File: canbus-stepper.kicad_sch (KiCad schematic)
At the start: 63 parts, among them J1 TYPE-C USB SOCKET, J2 Motor Output, J3 CAN Daisy-Chain 1, J4 CAN Daisy-Chain 2, J5 Qwiic I2C, J6 AUX Port, J7 SFV30R-2STBE1HLF (30-Pin OLED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, J8 24V Power Input Terminal, J9 24V Power Output Terminal, Q1 AO4407A, SW1 SW_Push, SW2 SW_Push, SW3 SW_Push, SW4 SW_Push, U1 ESP32-S3-WROOM-1, U2 TMC2209, U3 AS5600-ASOT, U4 TCAN1051VDRBTQ1, U5 MP2315, U6 AP2112K-3.3TRG1, U7 USBLC6-2SC6

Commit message: chore: save board and schematic progress before autoplacer development
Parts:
- added SW5: Termination, CANBUS-Stepper:SW_TS31-46-35-BK-B-160-RA-SMT-TR, symbol Switch:SW_Push
- U1: value ESP32-S3-WROOM-1 -> ESP32-S3-MINI-1; symbol MCU_Module:ESP32-S3-WROOM-1 -> MCU_Module:ESP32-S3-MINI-1
- U4: symbol Interface_CAN:SN65HVD230 -> Interface_CAN:TCAN1051
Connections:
- net CAN_VREF is gone; now on net +3V3: U4.5 (VIO)
- net MS1 is gone; now on net GND: U2.9 (MS1)
- net MS2 is gone; now on net GND: U2.10 (MS2)
- net +3V3: now also U1.3 (3V3), U6.5 (VOUT); no longer U1.2 (3V3), U4.3 (VCC), U6.4 (VOUT)
- net +5V: now also U4.3 (VCC)
- net AUX1: now also U1.19 (IO14); no longer U1.22 (IO14)
- net AUX2: now also U1.18 (IO13); no longer U1.21 (IO13)
- net CANL: now also SW5.2
- net CAN_RX: now also U1.28 (IO47); no longer U1.24 (IO47)
- net CAN_STB: now also U1.37 (IO37); no longer U1.30 (IO37)
- net CAN_TERM_SW: now also SW5.1
- net CAN_TX: now also U1.31 (IO48); no longer U1.25 (IO48)
- net DIAG: now also U1.21 (IO16); no longer U1.9 (IO16)
- net DIR: now also U1.10 (IO6); no longer U1.6 (IO6)
- net DISABLE_3V3: now also U1.38 (IO38); no longer U1.31 (IO38)
- net EN: now also U1.39 (EN); no longer U1.3 (EN)
- net ENC_OUT_N: now also U3.5 (OUT_N); no longer U3.3 (OUT_N)
- net ENC_OUT_P: now also U3.3 (OUT_P); no longer U3.2 (OUT_P)
- net GND: now also U1.16 (GND), U3.2 (MODE); no longer U1.40 (GND), U1.41 (GND_PAD), U3.5 (GND)
- net INDEX: now also U1.15 (IO11); no longer U1.19 (IO11)
- net IO0: now also U1.4 (IO0); no longer U1.27 (IO0)
- net IO46: now also U1.46 (GND); no longer U1.16 (IO46)
- net LED1: now also U1.14 (IO10); no longer U1.18 (IO10)
- net LED2: now also U1.17 (IO12); no longer U1.20 (IO12)
- net NTC_SENSE: now also U1.11 (IO7); no longer U1.7 (IO7)
- net SCL: now also U1.13 (IO9), U3.7 (SCL); no longer U1.17 (IO9), U3.6 (SCL)
- net SDA: now also U3.6 (SDA); no longer U3.7 (SDA)
- net STEP: now also U1.9 (IO5); no longer U1.5 (IO5)
- net SW1: now also U1.35 (IO35); no longer U1.28 (IO35)
- net SW2: now also U1.36 (IO36); no longer U1.29 (IO36)
- net TMC_EN: now also U1.26 (NC); no longer U1.23 (IO21)
- net TMC_RX: now also U1.23 (IO18); no longer U1.11 (IO18)
- net TMC_TX: now also U1.22 (IO17); no longer U1.10 (IO17)
- net USB_D+: now also U1.25 (IO20); no longer U1.14 (IO20)
- net USB_D-: now also U1.24 (IO19); no longer U1.13 (IO19)
- net VBUS_SENSE: now also U1.8 (NC); no longer U1.4 (IO4)
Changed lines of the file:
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@@
 		)
 	)
-	(label "MS1"
+	(label "GND"
 		(at 299.72 76.2 0)
 		(effects
@@
 		)
 	)
-	(label "MS2"
+	(label "GND"
 		(at 299.72 78.74 0)
 		(effects
@@
 		)
 	)
-	(label "CAN_VREF"
+	(label "+3V3"
 		(at 326.07 199.23 0)
 		(effects
@@
 	)
 	(symbol
-		(lib_id "Interface_CAN:SN65HVD230")
+		(lib_id "Interface_CAN:TCAN1051")
 		(at 315.91 194.15 0)
 		(unit 1)
@@
 	)
 	(symbol
-		(lib_id "power:+3V3")
+		(lib_id "power:+5V")
 		(at 305.75 199.23 0)
 		(unit 1)
@@
 			)
 		)
-		(property "Value" "+3V3"
+		(property "Value" "+5V"
 			(at 305.75 196.23 0)
 			(show_name no)
@@
 	)
 	(symbol
-		(lib_id "MCU_Module:ESP32-S3-WROOM-1")
+		(lib_id "MCU_Module:ESP32-S3-MINI-1")
 		(at 152.4 85.09 0)
 		(unit 1)
@@
 			)
 		)
-		(property "Value" "ESP32-S3-WROOM-1"
+		(property "Value" "ESP32-S3-MINI-1"
 			(at 152.4 100.09 0)
 			(show_name no)
@@
 	(label "+24V_IN" (at 80.01 194.31 0) (effects (font (size 1.27 1.27))))
 	(label "USB_VBUS_RAW" (at 65.73 83.98 0) (effects (font (size 1.27 1.27))))
+	(symbol
+		(lib_id "Switch:SW_Push")
+		(at 350 197.96 0)
+		(unit 1)
+		(body_style 1)
+		(exclude_from_sim no)
+		(in_bom yes)
+		(on_board yes)
+		(in_pos_files yes)
+		(dnp no)
+		(property "Reference" "SW5"
+			(at 350 182.96 0)
+			(show_name no)
+			(do_not_autoplace no)
+			(effects
+				(font
+					(size 1.27 1.27)
+				)
+			)
+		)
+		(property "Value" "Termination"
+			(at 350 212.96 0)
+			(show_name no)
+			(do_not_autoplace no)
+			(effects
+				(font
+					(size 1.27 1.27)
+				)
+			)
+		)
+		(property "Footprint" "CANBUS-Stepper:SW_TS31-46-35-BK-B-160-RA-SMT-TR"
+			(at 350 197.96 0)
+			(hide yes)
+			(show_name no)
+			(do_not_autoplace no)
+			(effects
+				(font
+					(size 1.27 1.27)
+				)
+			)
+		)
+		(property "Datasheet" "~"
+			(at 350 197.96 0)
+			(hide yes)
+			(show_name no)
+			(do_not_autoplace no)
+			(effects
+				(font
+					(size 1.27 1.27)
+				)
+			)
+		)
+		(property "Description" "CAN Bus 120R Termination Switch"
+			(at 350 197.96 0)
+			(show_name no)
+			(do_not_autoplace no)
+			(effects
+				(font
+					(size 1.27 1.27)
+				)
+			)
+		)
+		(pin "1"
+		)
+		(pin "2"
+		)
+		(instances
+			(project "canbus-stepper"
+				(path "/708095da-6de2-439a-99a4-e77d5d456b3f"
+					(reference "SW5")
+					(unit 1)
+				)
+			)
+		)
+	)
+	(label "CAN_TERM_SW"
+		(at 344.92 197.96 0)
+		(effects
+			(font
+				(size 1.27 1.27)
+			)
+		)
+	)
+	(label "CANL"
+		(at 355.08 197.96 0)
+		(effects
+			(font
+				(size 1.27 1.27)
+			)
+		)
+	)
 )

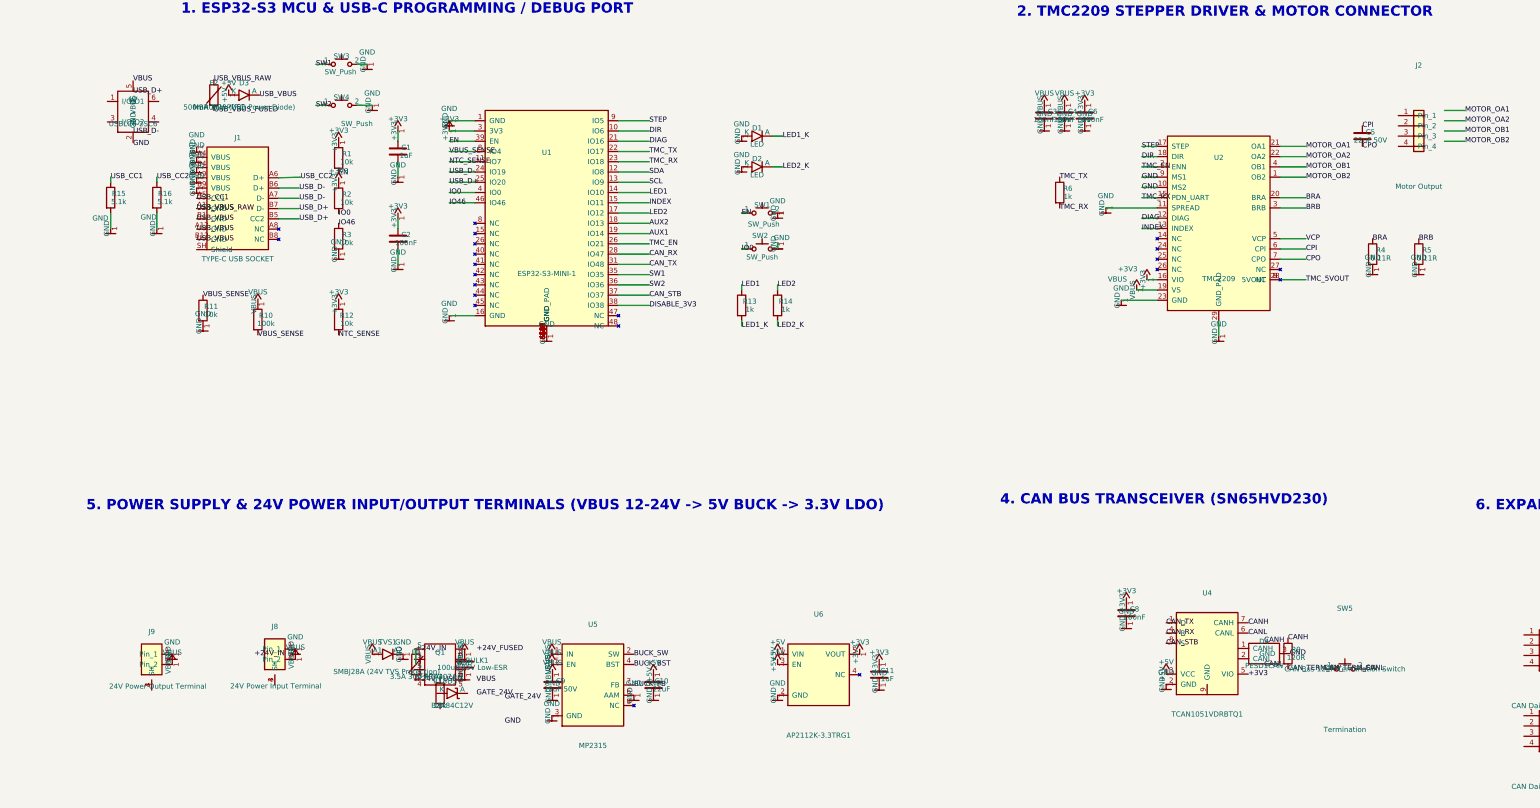
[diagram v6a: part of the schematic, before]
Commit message: update canbus ohm sw footprint
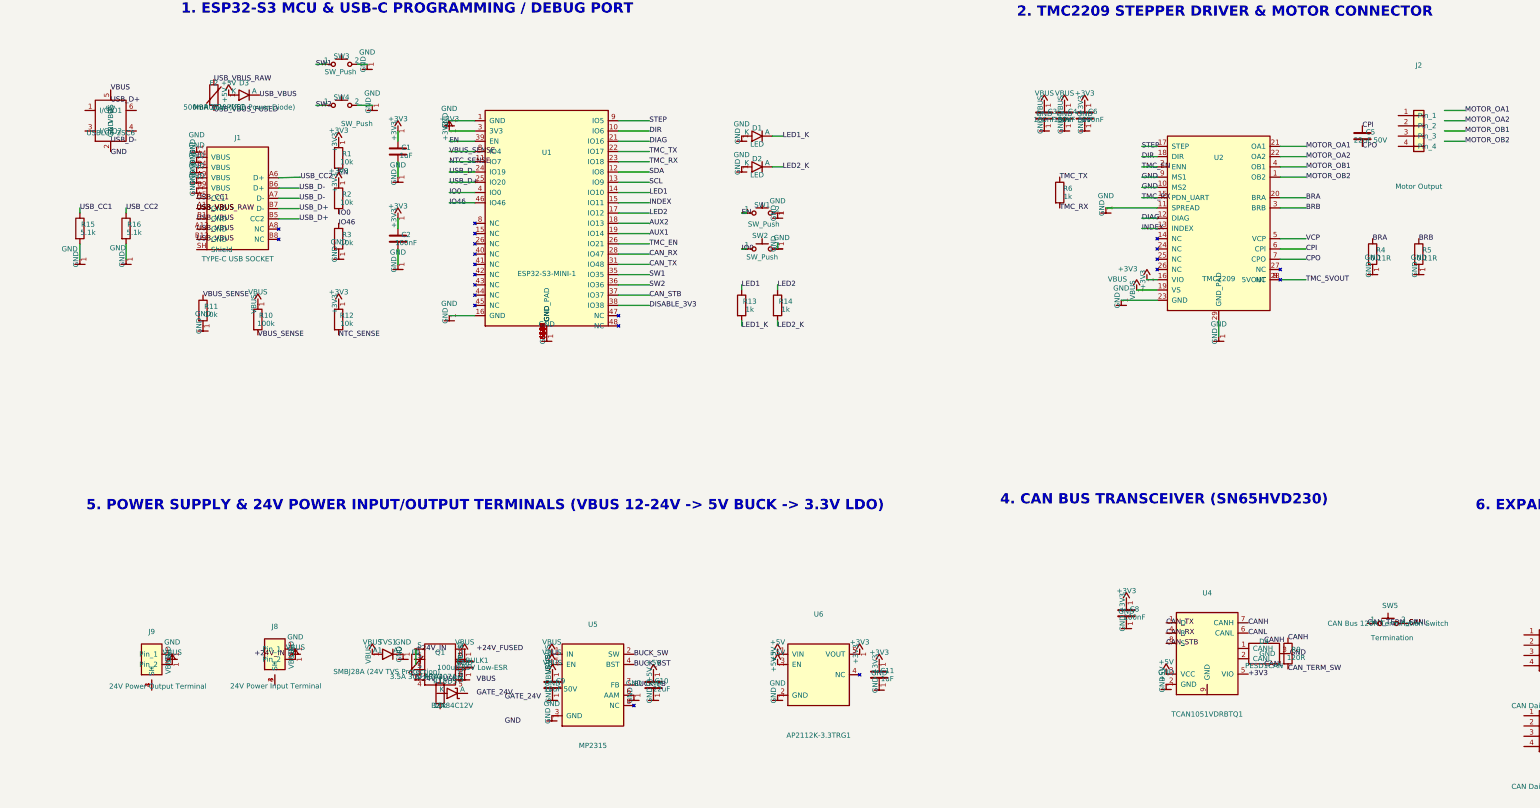
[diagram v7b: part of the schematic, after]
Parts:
- SW5: footprint CANBUS-Stepper:SW_TS31-46-35-BK-B-160-RA-SMT-TR -> Button_Switch_SMD:SW_DIP_SPSTx01_Slide_Copal_CHS-01A_W5.08mm_P1.27mm_JPin
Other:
- moved on the sheet: R15, R16, SW5, U7

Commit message: full revision of net connection, components
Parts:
- removed D5: BZX84C12V, Diode_SMD:D_SOD-123, symbol Device:D_Zener
- removed J1: TYPE-C USB SOCKET, CANBUS-Stepper:USB_C_Receptacle_16P, symbol Connector:USB_C_Receptacle
- removed J3: CAN Daisy-Chain 1, Connector_JST:JST_SH_SM04B-SRSS-TB_1x04-1MP_P1.00mm_Horizontal, symbol Connector:Conn_01x04
- removed J4: CAN Daisy-Chain 2, Connector_JST:JST_SH_SM04B-SRSS-TB_1x04-1MP_P1.00mm_Horizontal, symbol Connector:Conn_01x04
- removed J8: 24V Power Input Terminal, CANBUS-Stepper:CONN_SD-43650-005_02_MOL, symbol Connector:Conn_01x02
- removed J9: 24V Power Output Terminal, CANBUS-Stepper:CONN_SD-43650-005_02_MOL, symbol Connector:Conn_01x02
- removed Q1: AO4407A, Package_SO:SOIC-8_3.9x4.9mm_P1.27mm, symbol Device:Q_PMOS_GDS
- removed U1: ESP32-S3-MINI-1, CANBUS-Stepper:XCVR_ESP32-S3-MINI-1-N4R2, symbol MCU_Module:ESP32-S3-MINI-1
- removed U2: TMC2209, Package_DFN_QFN:QFN-28-1EP_5x5mm_P0.5mm_EP3.25x3.25mm, symbol Driver_Motor:TMC2209
- removed U3: AS5600-ASOT, Package_SO:SOIC-8_3.9x4.9mm_P1.27mm, symbol Sensor_Magnetic:MT6701
- removed U4: TCAN1051VDRBTQ1, CANBUS-Stepper:TCAN1051VDRBTQ1, symbol Interface_CAN:TCAN1051
- removed U5: MP2315, Package_TO_SOT_SMD:SOT-23-8, symbol Regulator_Switching:MP2315
- removed U6: AP2112K-3.3TRG1, Package_TO_SOT_SMD:SOT-23-5, symbol Regulator_Linear:ME6211C33
- added C16: 1uF, Capacitor_SMD:C_0805_2012Metric, symbol Device:C
- added D6: BZX84Cxx, Package_TO_SOT_SMD:SOT-23, symbol Diode:BZX84Cxx
- added D7: LED, LED_SMD:LED_0805_2012Metric, symbol Device:LED
- added IC1: AS5600-ASOT, CANBUS-Stepper:AS5600-ASOT, symbol AS5600-ASOT:AS5600-ASOT
- added J1: USB_C_Receptacle_USB2.0_16P, CANBUS-Stepper:USB_C_Receptacle_16P, symbol Connector:USB_C_Receptacle_USB2.0_16P
- added J10, J11: SM02B-SRSS-TB_LF__SN_, CANBUS-Stepper:SM02B-SRSS-TB_LF__SN_, symbol SM02B-SRSS-TB_LF__SN_:SM02B-SRSS-TB_LF__SN_
- added J3, J4: 436500209, CANBUS-Stepper:MOLEX_436500209, symbol 436500209:436500209
- added L1: 4.7uH, Inductor_SMD:L_0603_1608Metric, symbol Device:L
- added Q2: FDS9435A, Package_SO:SOIC-8_3.9x4.9mm_P1.27mm, symbol Transistor_FET:FDS9435A
- added R19: 1k, Resistor_SMD:R_0603_1608Metric, symbol Device:R
- added U1: ESP32-S3-MINI-1, RF_Module:ESP32-S2-MINI-1, symbol RF_Module:ESP32-S3-MINI-1
- added U2: TMC2209-LA, Package_DFN_QFN:VQFN-28-1EP_5x5mm_P0.5mm_EP3.7x3.7mm_ThermalVias, symbol Driver_Motor:TMC2209-LA
- added U3: AP2112K-3.3, Package_TO_SOT_SMD:SOT-23-5, symbol Regulator_Linear:AP2112K-3.3
- added U5: TCAN1044VDDFRQ1, CANBUS-Stepper:SOT65P280X110-8N, symbol TCAN1044VDDFRQ1:TCAN1044VDDFRQ1
- added U8: MP2315GJ, Package_TO_SOT_SMD:SOT-23-8, symbol MP2315GJ:MP2315GJ
- C6: value 100nF -> 10uF 50V; footprint Capacitor_SMD:C_0603_1608Metric -> Capacitor_SMD:C_1206_3216Metric
- D4: LCSC (none) -> PESD1CAN; Link (none) -> https://www.e-komponent.com/pesd1can-evvo-tvs-diyot
- J2: LCSC (none) -> S4B-PH-SM4-TB; Link (none) -> https://www.e-komponent.com/connector-header-surface-mount-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
- J7: LCSC (none) -> SFV30R-2STBE1HLF; Link (none) -> https://www.e-komponent.com/sfv30r-2stbe1hlf-amphenol-icc-f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
- SW1, SW2: LCSC (none) -> TL3365AF180QG; Link (none) -> https://www.e-komponent.com/eg5384ct-nd-e-switch-tactile-sw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
- SW3, SW4: LCSC (none) -> TS31-46-35-BK-B-160-RA-SMT-TR; Link (none) -> https://www.e-komponent.com/ts31-46-35-bk-b-160-ra-smt-tr-s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
- U7: LCSC (none) -> USBLC6-2SC6_UMW; Link (none) -> https://www.e-komponent.com/usblc6-2sc6-umw-ipp-tvs-diode
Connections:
- net +24V_FUSED: now also C3.2, C6.1, TVS1.1 (A1), D6.1 (A), Q2.1 (S), Q2.2 (S), Q2.3 (S), U2.22 (VS), U2.28 (VS)
- net +3V3: now also J5.2 (Pin_2), J6.2 (Pin_2), J7.18 (Pin_18), IC1.1 (VDD5V), IC1.2 (VDD3V3), U1.3 (3V3), U2.15 (VCC_IO), U2.17 (VREF), U3.5 (VOUT), U5.5 (VIO/NC); no longer C6.1, C8.1
- net +5V: now also C8.1, L1.2, U3.1 (VIN), U3.3 (EN), U5.3 (VCC); no longer D3.1 (K)
- net AUX1: now also J6.3 (Pin_3), U1.18 (IO14)
- net AUX2: now also J6.4 (Pin_4), U1.17 (IO13)
- net BRA: now also U2.23 (BRA)
- net BRB: now also U2.27 (BRB)
- net BUCK_BST: now also U8.5 (BST)
- net BUCK_FB: now also U8.8 (FB)
- net BUCK_SW: now also L1.1, U8.3 (SW)
- net CANH: now also D4.1 (CANH), J10.1, J11.1, U5.7 (CANH)
- net CANL: now also D4.2 (CANL), J10.2, J11.2, U5.6 (CANL)
- net CAN_RX: now also U1.27 (IO47), U5.4 (RXD)
- net CAN_STB: now also U1.33 (IO37), U5.8 (STB)
- net CAN_TX: now also U1.30 (IO48), U5.1 (TXD)
- net CPI: now also U2.5 (CPI)
- net CPO: now also U2.4 (CPO)
- net DIAG: now also U1.20 (IO16), U2.11 (DIAG)
- net DIR: now also U1.10 (IO6), U2.19 (DIR)
- net DISABLE_3V3: now also U1.34 (IO38)
- net EN: now also U1.45 (EN)
- net GATE_24V: now also R18.1, D6.3 (K), Q2.4 (G)
- net GND: now also J5.1 (Pin_1), J6.1 (Pin_1), J7.1 (Pin_1), R18.2, SW1.2, SW2.2, SW3.2, SW4.2, U7.2 (GND), C16.2, D7.2 (A), IC1.4 (GND), IC1.8 (DIR), J1.A1 (GND), J1.A12 (GND), J1.B1 (GND), J1.B12 (GND), J1.SH (SHIELD), J3.2, J3.S1 (SHIELD1), J3.S2 (SHIELD2), J4.2, J4.S1 (SHIELD1), J4.S2 (SHIELD2), U1.1 (GND), U1.2 (GND), U1.42 (GND), U1.43 (GND), U1.46 (GND), U1.47 (GND), U1.48 (GND), U1.49 (GND), U1.50 (GND), U1.51 (GND), U1.52 (GND), U1.53 (GND), U1.54 (GND), U1.55 (GND), U1.56 (GND), U1.57 (GND), U1.58 (GND), U1.59 (GND), U1.60 (GND), U1.61 (GND), U1.62 (GND), U1.63 (GND), U1.64 (GND), U1.65 (GND), U2.10 (MS2/AD1), U2.13 (CLK), U2.18 (GND), U2.20 (STDBY), U2.29 (GND), U2.3 (GND), U2.9 (MS1/AD0), U3.2 (GND), U5.2 (GND), U8.4 (GND); no longer C3.2, J7.18 (Pin_18)
- net INDEX: now also U1.15 (IO11), U2.12 (INDEX)
- net IO0: now also U1.4 (IO0)
- net IO46: now also U1.44 (IO46)
- net LED1: now also U1.14 (IO10)
- net LED2: now also U1.16 (IO12)
- net MOTOR_OA1: now also J2.1 (Pin_1), U2.24 (OA1)
- net MOTOR_OA2: now also J2.2 (Pin_2), U2.21 (OA2)
- net MOTOR_OB1: now also J2.3 (Pin_3), U2.26 (OB1)
- net MOTOR_OB2: now also J2.4 (Pin_4), U2.1 (OB2)
- net NTC_SENSE: now also U1.11 (IO7)
- net SCL: now also J5.4 (Pin_4), IC1.7 (SCL), U1.13 (IO9)
- net SDA: now also J5.3 (Pin_3), IC1.6 (SDA), U1.12 (IO8)
- net STEP: now also U1.9 (IO5), U2.16 (STEP)
- net SW1: now also SW3.1, U1.31 (IO35)
- net SW2: now also SW4.1, U1.32 (IO36)
- net TMC_5VOUT: now also C4.1, U2.8 (5VOUT)
- net TMC_EN: now also U1.25 (IO21), U2.2 (~{EN})
- net TMC_RX: now also U1.22 (IO18), U2.14 (~{PD}/UART)
- net TMC_TX: now also U1.21 (IO17)
- net USB_CC1: now also J1.A5 (CC1)
- net USB_CC2: now also J1.B5 (CC2)
- net USB_D+: now also U7.3 (I/O2), J1.A6 (D+), J1.B6 (D+), U1.24 (USB_D+)
- net USB_D-: now also U7.1 (I/O1), J1.A7 (D-), J1.B7 (D-), U1.23 (USB_D-)
- net USB_VBUS: now also D3.1 (K); no longer D3.2 (A)
- net USB_VBUS_FUSED: now also D3.2 (A), F2.2, R10.1, U7.5 (VBUS), R19.2
- net VBUS: now also Q2.5 (D), Q2.6 (D), Q2.7 (D), Q2.8 (D), U8.2 (IN), U8.6 (EN/SYNC); no longer C3.1, C4.1, R10.1, TVS1.1 (A1)
- net VBUS_SENSE: now also U1.8 (IO4)
- net VCP: now also C3.1, U2.6 (VCP)
- net USB_VBUS_RAW: now reaches F2.1
- net USB_VBUS_RAW: now also J1.A4 (VBUS), J1.A9 (VBUS), J1.B4 (VBUS), J1.B9 (VBUS)
- net MCU_USB_D_P: now reaches U7.4 (I/O2)
- net MCU_USB_D_N: now reaches U7.6 (I/O1)
- net +24V_IN renamed +24V_RAW
- net +24V_RAW: now also J3.1, J4.1
- net LED1_K: no longer names the net of D1.2 (A), R13.2
- net LED2_K: no longer names the net of D2.2 (A), R14.2
- new net AAM: U8.1 (AAM)
- new net USB_LED_LINE: D7.1 (K), R19.1
- new net VCC_5V_REG: C16.1, U8.7 (VCC)
- no-connect marks 0 -> 6
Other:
- moved on the sheet: C1, C10, C11, C12, C13, C14, C15, C2, C3, C4, C5, C6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
